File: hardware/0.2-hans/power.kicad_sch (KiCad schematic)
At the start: 27 parts, among them U2 ECP5U_25_CABGA256, U3 LP5907MFX-3.3, U4 LP5907MFX-2.5, U5 LP5907MFX-1.2

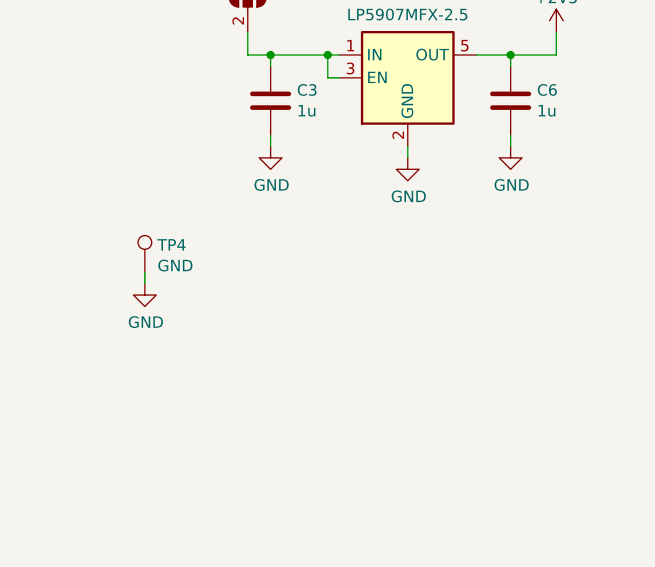
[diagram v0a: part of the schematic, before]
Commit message: remove usb, add 5v
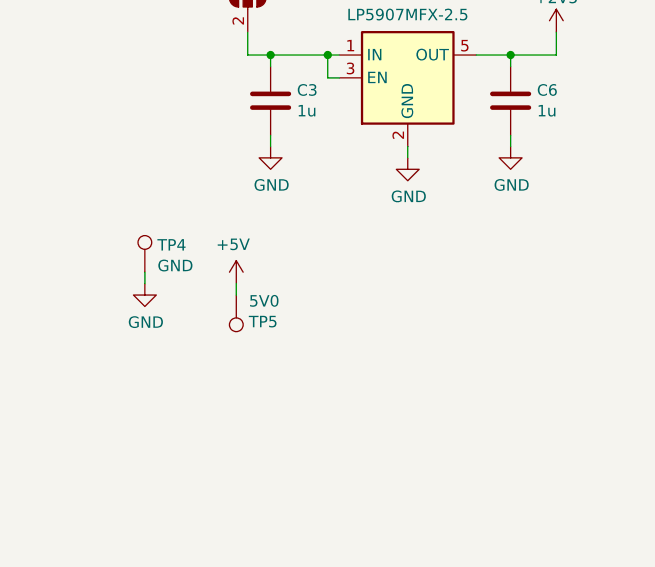
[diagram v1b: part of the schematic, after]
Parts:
- added TP5: 5V0, josh-test-point:Test-Point-Loop-RED, symbol Connector:TestPoint
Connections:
- net +5V: now also TP5.1
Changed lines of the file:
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@@
+    (stroke (width 0) (type solid) (color 0 0 0 0))
+  )
+  (wire (pts (xy 34.29 151.13) (xy 34.29 149.86))
     (stroke (width 0) (type solid) (color 0 0 0 0))
   )
@@
       (effects (font (size 1.27 1.27)) hide)
     )
+    (pin "1")
+  )
+  (symbol (lib_id "Connector:TestPoint") (at 34.29 151.13 0) (mirror x) (unit 1)
+    (in_bom no) (on_board yes)
+    (property "Reference" "TP5" (id 0) (at 35.6871 154.1209 0)
+      (effects (font (size 1.27 1.27)) (justify left))
+    )
+    (property "Value" "5V0" (id 1) (at 35.687 151.822 0)
+      (effects (font (size 1.27 1.27)) (justify left))
+    )
+    (property "Footprint" "josh-test-point:Test-Point-Loop-RED" (id 2) (at 39.37 151.13 0)
+      (effects (font (size 1.27 1.27)) hide)
+    )
+    (property "Datasheet" "~" (id 3) (at 39.37 151.13 0)
+      (effects (font (size 1.27 1.27)) hide)
+    )
+    (property "DNP" "DNP" (id 4) (at 34.29 151.13 0)
+      (effects (font (size 1.27 1.27)) hide)
+    )
+    (pin "1")
+  )
+  (symbol (lib_id "power:+5V") (at 34.29 149.86 0) (mirror y) (unit 1)
+    (in_bom yes) (on_board yes)
+    (property "Reference" "#PWR0116" (id 0) (at 34.29 153.67 0)
+      (effects (font (size 1.27 1.27)) hide)
+    )
+    (property "Value" "+5V" (id 1) (at 33.9217 145.5356 0))
+    (property "Footprint" "" (id 2) (at 34.29 149.86 0)
+      (effects (font (size 1.27 1.27)) hide)
+    )
+    (property "Datasheet" "" (id 3) (at 34.29 149.86 0)
+      (effects (font (size 1.27 1.27)) hide)
+    )
